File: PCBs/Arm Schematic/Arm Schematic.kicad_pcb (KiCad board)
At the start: 4 copper layers, 91.3 x 148 mm, 174 parts, among them J1 USB_C_Receptacle_USB2.0_16P, J10 Conn_01x02, J11 Conn_01x04, J12 Conn_01x04, J13 Conn_01x02, J15 Conn_01x04, J16 Conn_01x05, J17 Conn_01x03, J2 Conn_01x05, J21 Conn_01x03, J22 Conn_01x03, J23 Conn_01x02, J24 Conn_01x04, J3 Conn_01x05, J4 Conn_01x05, J5 Conn_01x05, J6 Conn_01x04, J7 Conn_01x02, J8 Conn_01x02, J9 Conn_01x02, SW1 SW_Push, SW2 SW_Push, U1 ESP32-S3, U2 USBLC6-2SC6, U4 TCA9548APWR, U5 TXB0108DQSR, U6 TXB0108DQSR, U7 ADS1115IDGS, U8 W25Q16JVSS, U9 AMS1117-3.3, Y1 Crystal_GND24

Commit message: Updated Arm PCB
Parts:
- removed the C1 at (110.4, 82.2)
- removed the C10 at (100.1, 70.0)
- removed the C11 at (102.1, 70.0)
- removed the C12 at (96.9, 75.8)
- removed the C13 at (89.0, 94.0)
- removed the C14 at (115.2, 72.4)
- removed the C15 at (115.2, 77.4)
- removed the C16 at (135.0, 83.5)
- removed the C17 at (94.5, 60.7)
- removed the C18 at (96.4, 68.2)
- removed the C19 at (106.8, 68.2)
- removed the C2 at (112.6, 82.2)
- removed the C20 at (107.1, 59.4)
- removed the C21 at (142.2, 87.6)
- removed the C3 at (108.7, 78.8)
- removed the C4 at (96.8, 80.4)
- removed the C5 at (96.8, 82.4)
- removed the C6 at (108.6, 72.8)
- removed the C7 at (110.6, 72.8)
- removed the C8 at (100.1, 66.5)
- removed the C9 at (102.1, 66.5)
- removed the D1 at (112.9, 95.5)
- removed the D2 at (92.7, 94.8)
- removed the D3 at (90.6, 83.2)
- removed J1 (x2): USB_C_Receptacle_USB2.0_16P, Connector_USB:USB_C_Receptacle_GCT_USB4105-xx-A_16P_TopMnt_Horizontal
- removed the J10 at (134.4, 101.6)
- removed the J11 at (107.2, 52.0)
- removed the J12 at (118.0, 52.0)
- removed the J13 at (93.7, 101.5)
- removed the J15 at (128.9, 52.0)
- removed the J16 at (160.5, 100.5)
- removed the J17 at (121.8, 83.7)
- removed the J2 at (160.6, 89.0)
- removed the J21 at (148.8, 52.0)
- removed the J22 at (139.1, 52.0)
- removed the J23 at (143.7, 101.5)
- removed the J24 at (85.5, 52.0)
- removed the J3 at (160.5, 77.4)
- removed the J4 at (160.5, 65.9)
- removed the J5 at (160.4, 54.4)
- removed the J6 at (96.3, 52.0)
- removed the J7 at (110.4, 101.6)
- removed the J8 at (118.4, 101.5)
- removed the J9 at (126.5, 101.6)
- removed the L1 at (104.0, 68.1)
- removed the R1 at (88.6, 79.2)
- removed the R10 at (134.3, 91.1)
- removed the R11 at (134.3, 87.7)
- removed the R12 at (137.7, 95.8)
- removed the R13 at (137.7, 93.9)
- removed the R14 at (142.2, 95.9)
- removed the R15 at (145.6, 95.9)
- removed the R16 at (149.0, 84.3)
- removed the R17 at (149.0, 87.9)
- removed the R18 at (149.0, 77.1)
- removed the R19 at (149.0, 80.7)
- removed the R2 at (89.6, 72.1)
- removed the R20 at (149.0, 69.8)
- removed the R21 at (149.0, 73.4)
- removed the R22 at (149.0, 62.6)
- removed the R23 at (149.0, 66.2)
- removed the R24 at (130.1, 76.6)
- removed the R25 at (130.2, 73.0)
- removed the R26 at (118.0, 94.4)
- removed the R27 at (120.9, 94.4)
- removed the R28 at (123.8, 94.4)
- removed the R29 at (126.8, 94.4)
- removed the R3 at (109.2, 95.5)
- removed the R4 at (89.1, 90.2)
- removed the R5 at (112.6, 75.0)
- removed the R6 at (140.2, 84.8)
- removed the R7 at (130.7, 87.2)
- removed the R8 at (130.8, 83.8)
- removed the R9 at (92.7, 91.4)
- removed the SW1 at (83.0, 62.0)
- removed the SW2 at (83.0, 92.0)
- removed the U1 at (103.1, 76.4)
- removed the U2 at (92.0, 76.8)
- removed the U4 at (137.9, 76.9)
- removed the U5 at (96.6, 64.2)
- removed the U6 at (107.0, 64.1)
- removed the U7 at (141.2, 91.8)
- removed the U8 at (101.6, 86.5)
- removed the U9 at (112.7, 88.3)
- removed the Y1 at (115.2, 74.9)
- added G***: LOGO, IPRL Footprints:IPRL_31mm, F.Cu at (132.0, 139.0)
- added J14: TYPE-C-31-M-12, IPRL Footprints:TYPE-C-31-M-12, F.Cu at (81.4, 155.0)
- D3: value D_Schottky -> MBRA340T3G; footprint Diode_SMD:D_0805_2012Metric -> Diode_SMD:D_SMA
- J13: footprint Connector_AMASS:AMASS_XT60-M_1x02_P7.20mm_Vertical -> Connector_AMASS:AMASS_XT30U-M_1x02_P5.0mm_Vertical
- Y1: footprint Oscillator:Oscillator_SMD_Abracon_ASDMB-4Pin_2.5x2.0mm -> Crystal:Crystal_SMD_SeikoEpson_FA238-4Pin_3.2x2.5mm
- moved H4 1.08 mm to (165.3, 186.0)
- moved Y1 0.60 mm to (117.1, 152.9)
- moved H2 0.57 mm to (83.3, 186.0)
- moved H3 0.54 mm to (165.3, 124.0)
- moved H1 0.53 mm to (83.9, 123.2)
- moved C14 0.36 mm to (116.8, 150.1)
- moved C15 0.30 mm to (116.6, 155.7)
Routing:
- net +5P: track 414.8 -> 219.6 mm, vias 22 -> 11
- net GND: track 201.5 -> 103.1 mm, vias 136 -> 148
- net /ESP_SDA: track 141.6 -> 70.8 mm
- net /ESP_SCL: track 133.7 -> 66.8 mm, vias 4 -> 2
- net /Servo_0: track 120.5 -> 63.7 mm, vias 4 -> 2
- net /Servo_1: track 104.4 -> 56.1 mm, vias 4 -> 2
- net /SC4: track 95.8 -> 49.8 mm
- net /IN2: track 97.3 -> 52.7 mm, vias 4 -> 2
- net /IN1: track 94.8 -> 51.5 mm, vias 4 -> 2
- net /ENA: track 92.3 -> 50.2 mm, vias 4 -> 2
- net /LS_3: track 90.9 -> 49.0 mm, vias 4 -> 2
- net /RESET: track 82.4 -> 41.2 mm, vias 4 -> 2
- net /SD4: track 81.2 -> 42.5 mm
- net +3.3V: track 104.2 -> 67.5 mm, vias 2 -> 14
- net /SDO: track 67.1 -> 33.0 mm
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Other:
- board size 91.3 x 148 mm -> 90 x 70 mm
- board text added: "5V"
- board text added: "Encoder Input"
- board text added: "External LEDs"
- board text added: "External Voltage"
- board text added: "Limit Switch Input"
- board text added: "Servo Input"
- board text added: "Stepper Input"
- board text added: "Wrist Input"

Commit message: Minor touch ups, arm complete
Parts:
- moved H1 1.00 mm to (83.3, 124.0)
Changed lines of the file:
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@@
 	(footprint "MountingHole:MountingHole_3.2mm_M3"
 		(layer "F.Cu")
-		(at 83.9 123.2)
+		(at 83.3 124)
 		(descr "Mounting Hole 3.2mm, no annular, M3")
 		(tags "mounting hole 3.2mm no annular m3")
@@
 			(at 0 -4.2 0)
 			(layer "F.SilkS")
+			(hide yes)
 			(effects
 				(font
@@
 	(via
 		(at 96.2 163.2)
-		(size 0.6)
+		(size 0.4)
 		(drill 0.3)
 		(layers "F.Cu" "B.Cu")
@@
 	(via
 		(at 97.2 161.9)
-		(size 0.6)
+		(size 0.4)
 		(drill 0.3)
 		(layers "F.Cu" "B.Cu")
@@
 	(via
 		(at 110.8 135.9)
-		(size 0.6)
+		(size 0.4)
 		(drill 0.3)
 		(layers "F.Cu" "B.Cu")
@@
 	(via
 		(at 109.4 163.1)
-		(size 0.6)
+		(size 0.4)
 		(drill 0.3)
 		(layers "F.Cu" "B.Cu")
@@
 	(via
 		(at 113.9 158.7)
-		(size 0.6)
+		(size 0.4)
 		(drill 0.3)
 		(layers "F.Cu" "B.Cu")
@@
 	(via
 		(at 103.4 142.9)
-		(size 0.6)
+		(size 0.4)
 		(drill 0.3)
 		(layers "F.Cu" "B.Cu")
@@
 	(via
 		(at 101.4 149.6)
-		(size 0.6)
+		(size 0.4)
 		(drill 0.3)
 		(layers "F.Cu" "B.Cu")
@@
 	(via
 		(at 88.8 141.9)
-		(size 0.6)
+		(size 0.4)
 		(drill 0.3)
 		(layers "F.Cu" "B.Cu")
@@
 	(via
 		(at 116 152.1)
-		(size 0.6)
+		(size 0.4)
 		(drill 0.3)
 		(layers "F.Cu" "B.Cu")
@@
 	(via
 		(at 142.1 159.2)
-		(size 0.6)
+		(size 0.4)
 		(drill 0.3)
 		(layers "F.Cu" "B.Cu")
@@
 	(via
 		(at 108.1 147.8)
-		(size 0.6)
+		(size 0.4)
 		(drill 0.3)
 		(layers "F.Cu" "B.Cu")
@@
 	(via
 		(at 87.7 158.2)
-		(size 0.6)
+		(size 0.4)
 		(drill 0.3)
 		(layers "F.Cu" "B.Cu")
@@
 	(via
 		(at 135.125 183)
-		(size 0.6)
+		(size 0.4)
 		(drill 0.3)
 		(layers "F.Cu" "B.Cu")
@@
 	(via
 		(at 96.6 153.8)
-		(size 0.6)
+		(size 0.4)
 		(drill 0.3)
 		(layers "F.Cu" "B.Cu")
@@
 	(via
 		(at 111.7 158.7)
-		(size 0.6)
+		(size 0.4)
 		(drill 0.3)
 		(layers "F.Cu" "B.Cu")
@@
 	(via
 		(at 96.3 160.4)
-		(size 0.6)
+		(size 0.4)
 		(drill 0.3)
 		(layers "F.Cu" "B.Cu")
@@
 	(via
 		(at 90.9 147.8)
-		(size 0.6)
+		(size 0.4)
 		(drill 0.3)
 		(layers "F.Cu" "B.Cu")
@@
 	(via
 		(at 93.275 154.8)
-		(size 0.6)
+		(size 0.4)
 		(drill 0.3)
 		(layers "F.Cu" "B.Cu")
@@
 	(via
 		(at 111.1 183)
-		(size 0.6)
+		(size 0.4)
 		(drill 0.3)
 		(layers "F.Cu" "B.Cu")
@@
 	(via
 		(at 127.2 183)
-		(size 0.6)
+		(size 0.4)
 		(drill 0.3)
 		(layers "F.Cu" "B.Cu")
@@
 	(via
 		(at 88.9 168)
-		(size 0.6)
+		(size 0.4)
 		(drill 0.3)
 		(layers "F.Cu" "B.Cu")
@@
 	(via
 		(at 119.1 183)
-		(size 0.6)
+		(size 0.4)
 		(drill 0.3)
 		(layers "F.Cu" "B.Cu")
@@
 	(via
 		(at 135.1 156.5)
-		(size 0.6)
+		(size 0.4)
 		(drill 0.3)
 		(layers "F.Cu" "B.Cu")
@@
 	(via
 		(at 97.6 148.1)
-		(size 0.6)
+		(size 0.4)
 		(drill 0.3)
 		(layers "F.Cu" "B.Cu")
@@
 	(via
 		(at 96.5 158.4)
-		(size 0.6)
+		(size 0.4)
 		(drill 0.3)
 		(layers "F.Cu" "B.Cu")
@@
 	(via
 		(at 118.1 155.4)
-		(size 0.6)
+		(size 0.4)
 		(drill 0.3)
 		(layers "F.Cu" "B.Cu")
@@
 	(via
 		(at 108.4 135.3)
-		(size 0.6)
+		(size 0.4)
 		(drill 0.3)
 		(layers "F.Cu" "B.Cu")
@@
 	(via
 		(at 87.5 151.8)
-		(size 0.6)
+		(size 0.4)
 		(drill 0.3)
 		(layers "F.Cu" "B.Cu")
@@
 	(via
 		(at 90.3 158.1)
-		(size 0.6)
+		(size 0.4)
 		(drill 0.3)
 		(layers "F.Cu" "B.Cu")
@@
 	(via
 		(at 108.7 139.7)
-		(size 0.6)
+		(size 0.4)
 		(drill 0.3)
 		(layers "F.Cu" "B.Cu")
@@
 	(via
 		(at 136.3 163.5)
-		(size 0.6)
+		(size 0.4)
 		(drill 0.3)
 		(layers "F.Cu" "B.Cu")
@@
 	(via
 		(at 104.8 169.5)
-		(size 0.6)
+		(size 0.4)
 		(drill 0.3)
 		(layers "F.Cu" "B.Cu")
@@
 	(via
 		(at 143.444484 157.955515)
-		(size 0.6)
+		(size 0.4)
 		(drill 0.3)
 		(layers "F.Cu" "B.Cu")
@@
 	(via
 		(at 115 150.4)
-		(size 0.6)
+		(size 0.4)
 		(drill 0.3)
 		(layers "F.Cu" "B.Cu")
@@
 	(via
 		(at 110 158.5)
-		(size 0.6)
+		(size 0.4)
 		(drill 0.3)
 		(layers "F.Cu" "B.Cu")
@@
 	(via
 		(at 91.8 172.8)
-		(size 0.6)
+		(size 0.4)
 		(drill 0.3)
 		(layers "F.Cu" "B.Cu")
@@
 	(via
 		(at 101.4 142.9)
-		(size 0.6)
+		(size 0.4)
 		(drill 0.3)
 		(layers "F.Cu" "B.Cu")
@@
 	)
 	(segment
+		(start 107.82 152.2)
+		(end 107.82 151.8)
+		(width 0.2)
+		(layer "F.Cu")
+		(net 3)
+	)
+	(segment
 		(start 151.2125 165.9)
 		(end 152 165.9)
@@
 	(via
 		(at 119.7 169.4)
-		(size 0.6)
+		(size 0.4)
 		(drill 0.3)
 		(layers "F.Cu" "B.Cu")
@@
 	(via
 		(at 106.692344 147.592344)
-		(size 0.6)
+		(size 0.4)
 		(drill 0.3)
 		(layers "F.Cu" "B.Cu")
@@
 	(via
 		(at 95.851473 154.8)
-		(size 0.6)
+		(size 0.4)
 		(drill 0.3)
 		(layers "F.Cu" "B.Cu")
@@
 	(via
 		(at 90.1 159.2)
-		(size 0.6)
+		(size 0.4)
 		(drill 0.3)
 		(layers "F.Cu" "B.Cu")
@@
 	(via
 		(at 104.1 159.3)
-		(size 0.6)
+		(size 0.4)
 		(drill 0.3)
 		(layers "F.Cu" "B.Cu")
@@
 	(via
 		(at 103.7 162.3)
-		(size 0.6)
+		(size 0.4)
 		(drill 0.3)
 		(layers "F.Cu" "B.Cu")
@@
 	(via
 		(at 102.051031 150.064934)
-		(size 0.6)
+		(size 0.4)
 		(drill 0.3)
 		(layers "F.Cu" "B.Cu")
@@
 	(via
 		(at 105.4 143.3)
-		(size 0.6)
+		(size 0.4)
 		(drill 0.3)
 		(layers "F.Cu" "B.Cu")
@@
 	(via
 		(at 107.256455 144.088435)
-		(size 0.6)
+		(size 0.4)
 		(drill 0.3)
 		(layers "F.Cu" "B.Cu")
@@
 	(via
 		(at 109.5 145.1)
-		(size 0.6)
+		(size 0.4)
 		(drill 0.3)
 		(layers "F.Cu" "B.Cu")
@@
 	(via
 		(at 101.869998 155.4)
-		(size 0.6)
+		(size 0.4)
 		(drill 0.3)
 		(layers "F.Cu" "B.Cu")
@@
 	(via
 		(at 97.1125 144.029771)
-		(size 0.6)
+		(size 0.4)
 		(drill 0.3)
 		(layers "F.Cu" "B.Cu")
@@
 	(via
 		(at 110.3 144.3)
-		(size 0.6)
+		(size 0.4)
 		(drill 0.3)
 		(layers "F.Cu" "B.Cu")
@@
 	(via
 		(at 101.930145 156.637759)
-		(size 0.6)
+		(size 0.4)
 		(drill 0.3)
 		(layers "F.Cu" "B.Cu")
@@
 	(via
 		(at 106.1 143.9)
-		(size 0.6)
+		(size 0.4)
 		(drill 0.3)
 		(layers "F.Cu" "B.Cu")
@@
 	(via
 		(at 108.712847 144.235682)
-		(size 0.6)
+		(size 0.4)
 		(drill 0.3)
 		(layers "F.Cu" "B.Cu")
@@
 	(via
 		(at 102.3 159.4)
-		(size 0.6)
+		(size 0.4)
 		(drill 0.3)
 		(layers "F.Cu" "B.Cu")
@@
 	(via
 		(at 103.5 163.7)
-		(size 0.6)
+		(size 0.4)
 		(drill 0.3)
 		(layers "F.Cu" "B.Cu")
@@
 	)
 	(segment
-		(start 102.97 157.85)
-		(end 102.97 159.271449)
+		(start 102.935 161.670552)
+		(end 100.995 163.610552)
 		(width 0.2)
 		(layer "F.Cu")
@@
 	)
 	(segment
-		(start 102.97 159.271449)
-		(end 102.935 159.306449)
+		(start 102.97 157.85)
+		(end 102.97 159.271449)
 		(width 0.2)
 		(layer "F.Cu")
@@
 	)
 	(segment
-		(start 102.935 161.670552)
-		(end 100.995 163.610552)
+		(start 100.995 163.610552)
+		(end 100.995 168.1)
 		(width 0.2)
 		(layer "F.Cu")
@@
 	)
 	(segment
-		(start 100.995 163.610552)
-		(end 100.995 168.1)
+		(start 102.97 159.271449)
+		(end 102.935 159.306449)
 		(width 0.2)
 		(layer "F.Cu")

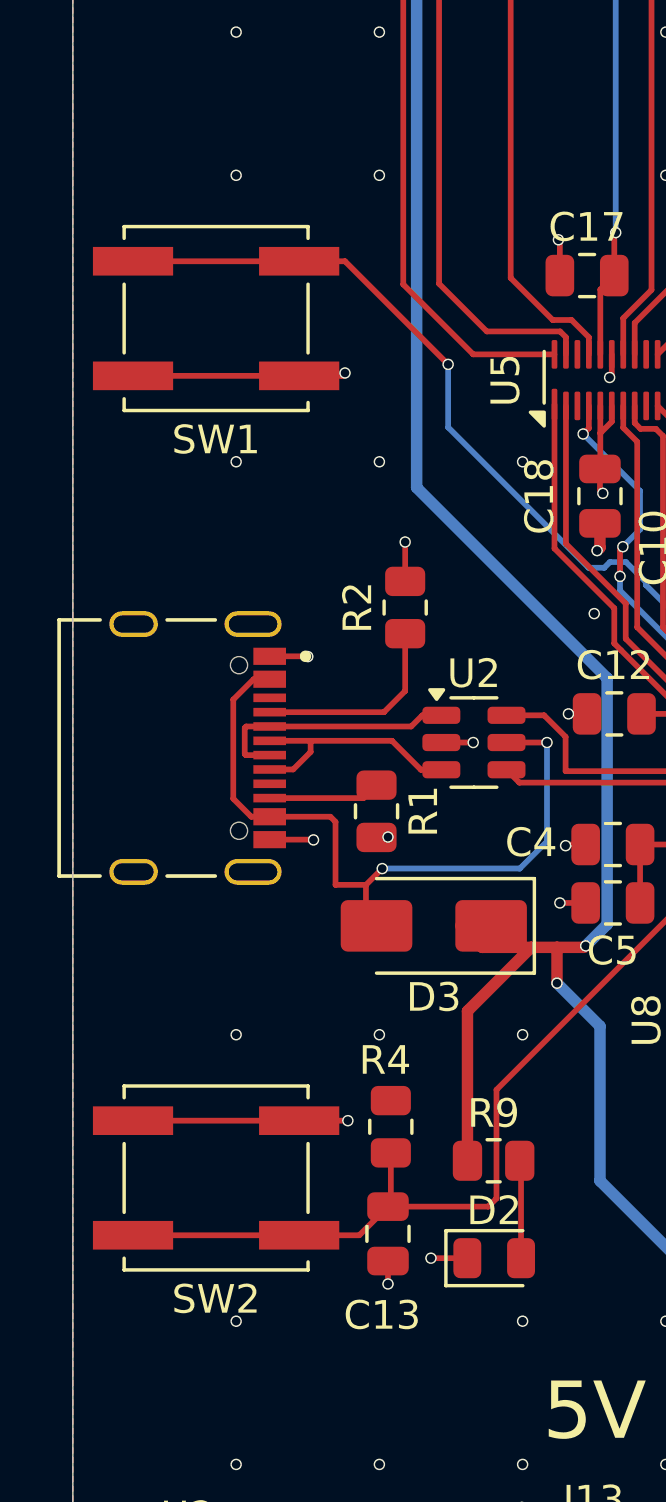
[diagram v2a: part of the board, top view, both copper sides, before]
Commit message: Added labels for buttons
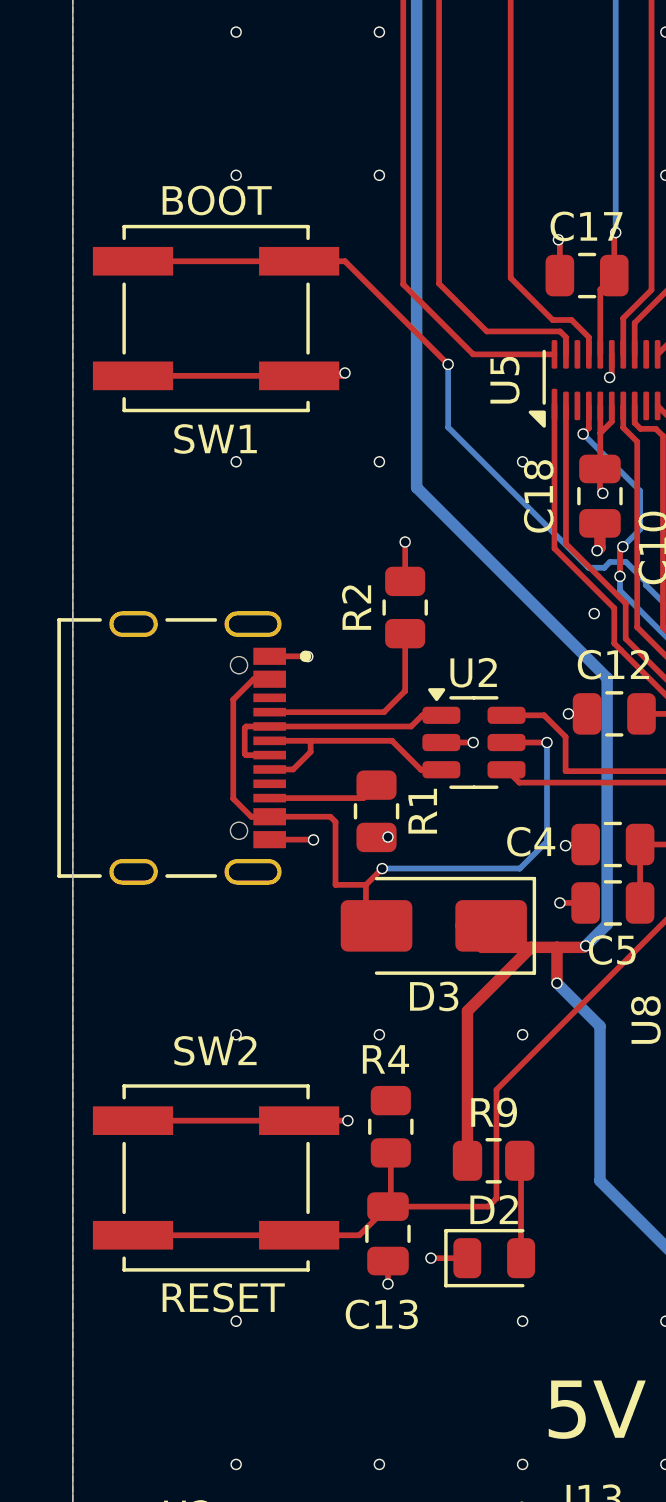
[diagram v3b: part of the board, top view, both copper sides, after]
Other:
- board text added: "BOOT"
- board text added: "RESET"
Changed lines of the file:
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@@
 		(tags "tactile switch ksc6")
 		(property "Reference" "SW2"
-			(at 0 4.24 0)
+			(at 0 -4.4 0)
 			(layer "F.SilkS")
 			(effects
@@
 		(layer "F.SilkS")
 		(effects
+			(font
+				(size 1 1)
+				(thickness 0.1)
+			)
+			(justify left bottom)
+		)
+	)
+	(gr_text "RESET"
+		(at 82.3 174.8 0)
+		(layer "F.SilkS")
+		(effects
+			(font
+				(size 1 1)
+				(thickness 0.1)
+			)
+			(justify left bottom)
+		)
+	)
+	(gr_text "BOOT"
+		(at 82.3 136.5 0)
+		(layer "F.SilkS")
+		(effects

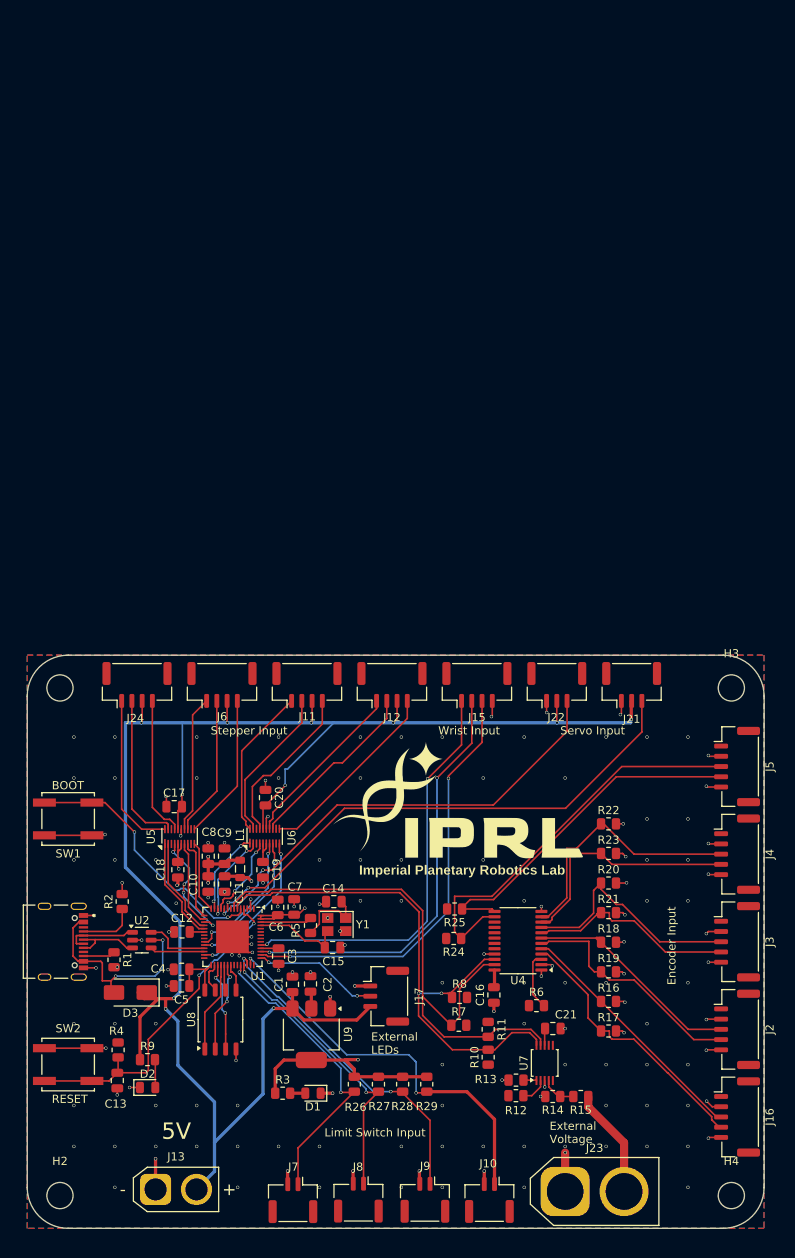
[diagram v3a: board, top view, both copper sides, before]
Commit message: Manufacturing data created + added names to PCBs.
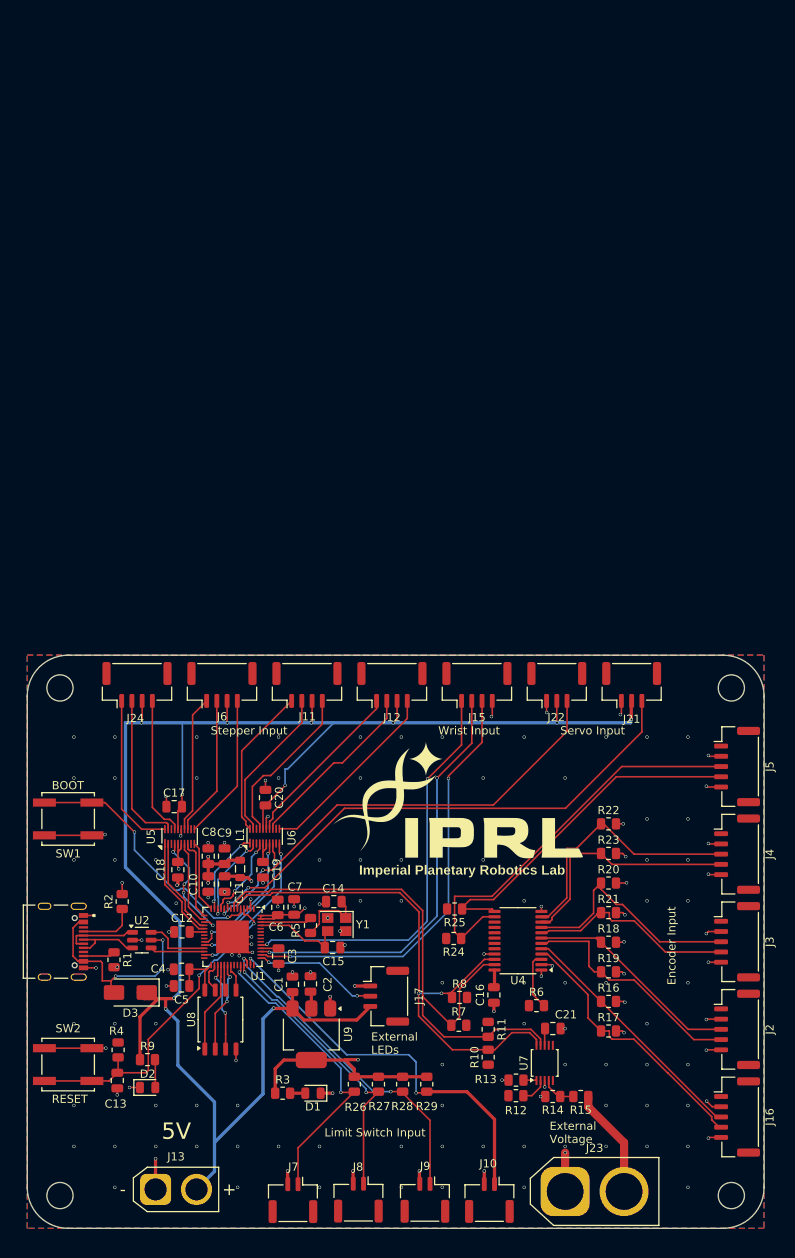
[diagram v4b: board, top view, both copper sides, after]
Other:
- board text added: "Arm Board"
- board text added: "Samuel Osebeyo"
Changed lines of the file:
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@@
 			(plotinvisibletext no)
 			(sketchpadsonfab no)
-			(subtractmaskfromsilk no)
+			(subtractmaskfromsilk yes)
 			(outputformat 1)
 			(mirror no)
-			(drillshape 1)
+			(drillshape 0)
 			(scaleselection 1)
-			(outputdirectory "")
+			(outputdirectory "output/")
 		)
 	)
@@
 			(at 0 -4.2 0)
 			(layer "F.SilkS")
+			(hide yes)
 			(effects
 				(font
@@
 			(at 0 -4.2 0)
 			(layer "F.SilkS")
+			(hide yes)
 			(effects
 				(font
@@
 			(at 0 -4.2 0)
 			(layer "F.SilkS")
+			(hide yes)
 			(effects
 				(font
@@
 		(layer "Edge.Cuts")
 	)
+	(gr_text "Samuel Osebeyo"
+		(at 150 141 0)
+		(layer "B.SilkS")
+		(effects
+			(font
+				(size 1.5 1.5)
+				(thickness 0.3)
+				(bold yes)
+			)
+			(justify left bottom mirror)
+		)
+	)
+	(gr_text "Arm Board\n"
+		(at 160 136 0)
+		(layer "B.SilkS" knockout)
+		(effects
+			(font
+				(size 5 5)
+				(thickness 0.75)
+			)
+			(justify left bottom mirror)
+		)
+	)
 	(gr_text "Limit Switch Input"
